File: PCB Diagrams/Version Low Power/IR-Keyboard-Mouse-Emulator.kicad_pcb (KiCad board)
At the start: 2 copper layers, 61 x 38.1 mm, 17 parts, among them J1 USB_A, J2 01x02, Q1 2N7000, Q2 BC547, U1 Arduino_Pro_Micro, U2 VS1838B

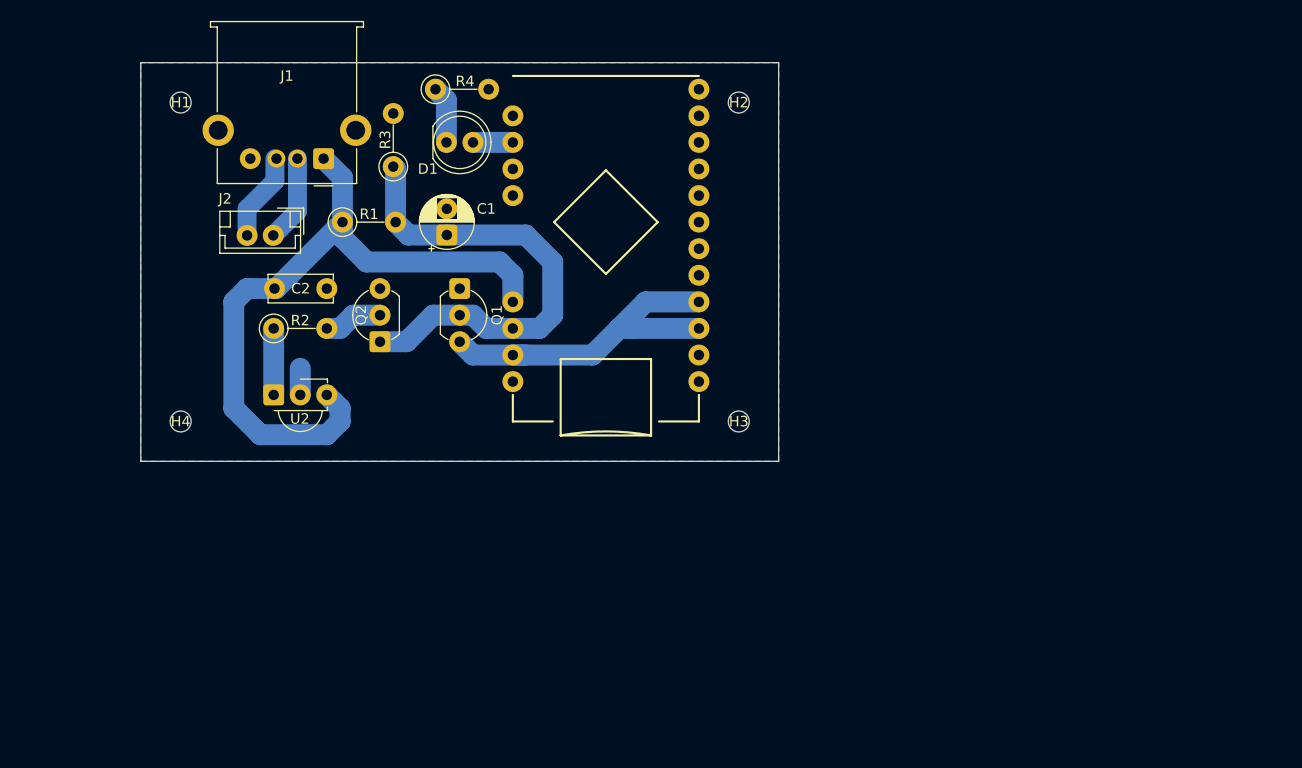
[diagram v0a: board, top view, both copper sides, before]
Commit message: Adding low-power firmware
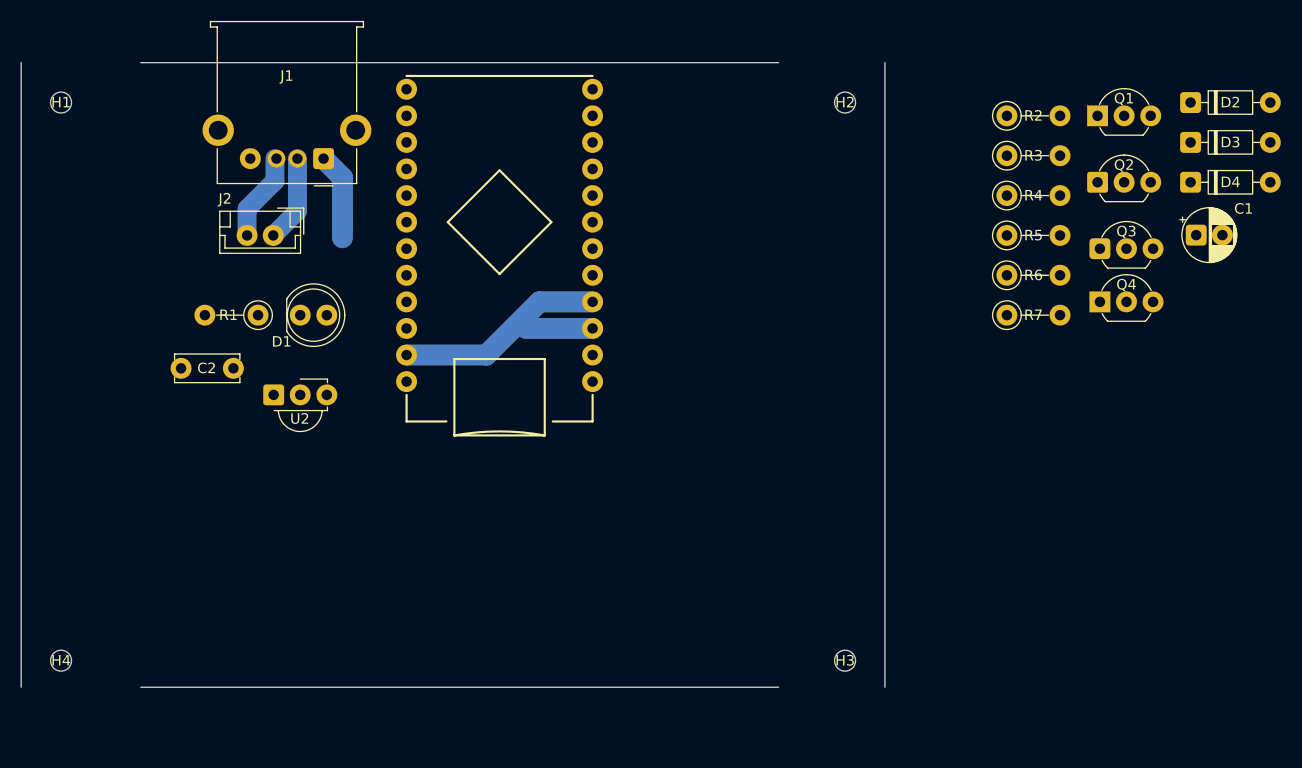
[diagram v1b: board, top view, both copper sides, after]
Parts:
- removed the R1 at (122.1, 64.8)
- added D2: 1N5817, Diode_THT:D_DO-35_SOD27_P7.62mm_Horizontal, F.Cu at (203.2, 53.3)
- added D3: 1N5817, Diode_THT:D_DO-35_SOD27_P7.62mm_Horizontal, F.Cu at (203.2, 57.1)
- added D4: 1N5817, Diode_THT:D_DO-35_SOD27_P7.62mm_Horizontal, F.Cu at (203.2, 61.0)
- added Q3: BC557, Package_TO_SOT_THT:TO-92_Inline_Wide, F.Cu at (194.5, 67.3)
- added Q4: BC547, Package_TO_SOT_THT:TO-92_Inline_Wide, F.Cu at (194.5, 72.4)
- added R4: 100K, Resistor_THT:R_Axial_DIN0207_L6.3mm_D2.5mm_P5.08mm_Vertical, F.Cu at (185.6, 62.2)
- added R5: 10K, Resistor_THT:R_Axial_DIN0207_L6.3mm_D2.5mm_P5.08mm_Vertical, F.Cu at (185.6, 66.0)
- added R6: 4.7K, Resistor_THT:R_Axial_DIN0207_L6.3mm_D2.5mm_P5.08mm_Vertical, F.Cu at (185.6, 69.8)
- added R7: 4.7K, Resistor_THT:R_Axial_DIN0207_L6.3mm_D2.5mm_P5.08mm_Vertical, F.Cu at (185.6, 73.7)
- C1: value 22uF -> 10uF
- Q1: value 2N7000 -> BC557
- R2: value 10K -> 47K
- R3: value 1M -> 10K
- moved R2 73.0 mm to (185.6, 54.6)
- moved C1 71.6 mm to (203.7, 66.0), turned to 0 degrees
- moved Q2 70.3 mm to (194.3, 61.0), turned to 0 degrees
- moved Q1 63.2 mm to (194.3, 54.6), turned to 0 degrees
- moved R3 58.7 mm to (185.6, 58.4), turned to 0 degrees
- moved R1 27.5 mm to (114.1, 73.7), turned to 180 degrees
- moved H4 25.6 mm to (95.2, 106.7)
- moved H3 25.0 mm to (170.2, 106.7)
- moved D1 21.6 mm to (118.1, 73.7)
- moved C2 15.9 mm to (106.7, 78.7), turned to 0 degrees
- moved H1 11.4 mm to (95.2, 53.3)
- moved H2 10.2 mm to (170.2, 53.3)
- moved U1 10.2 mm to (137.2, 67.3)
- renumbered R4 to R1
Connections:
- C1 pad 1: Net-(Q1-G) -> Net-(D4-A)
- Q1 pad 1: GND -> Net-(D4-A)
- Q1 pad 2: Net-(Q1-G) -> Net-(Q1-B)
- Q1 pad 3: GND_U1 -> +5V
- Q2 pad 1: Net-(Q1-G) -> Net-(Q2-C)
- Q2 pad 2: Net-(Q2-B) -> Net-(D2-K)
- R2 pad 2: Net-(Q2-B) -> Net-(Q1-B)
- R3 pad 1: Net-(Q1-G) -> Net-(D2-A)
- R3 pad 2: GND -> Net-(D4-A)
- U1 pad 21: +5V -> VCC
- U1 pad 23: GND_U1 -> GND
- U1 pad 3: GND_U1 -> GND
- U1 pad 4: GND_U1 -> GND
- U1 pad 7: unconnected-(U1-D4/A6-Pad7) -> DISCH
- U1 pad 8: unconnected-(U1-D5-Pad8) -> ON_OFF
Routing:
- net +5V: track 67.1 -> 8.31 mm
- net Net-(Q1-G): track 45.7 -> 0.00 mm
- net GND_U1: track 34.4 -> 0.00 mm
- net GND: track 2.54 -> 26.2 mm
- net IR_OUT: track 6.35 -> 0.00 mm
- net Net-(Q2-B): track 5.61 -> 0.00 mm
- net Net-(D1-K): track 5.51 -> 0.00 mm
- net Net-(D1-A): track 3.81 -> 0.00 mm
- removed copper zone on B.Cu, net GND
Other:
- board size 61 x 38.1 mm -> 82.6 x 59.7 mm

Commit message: Adding low-power version PCB
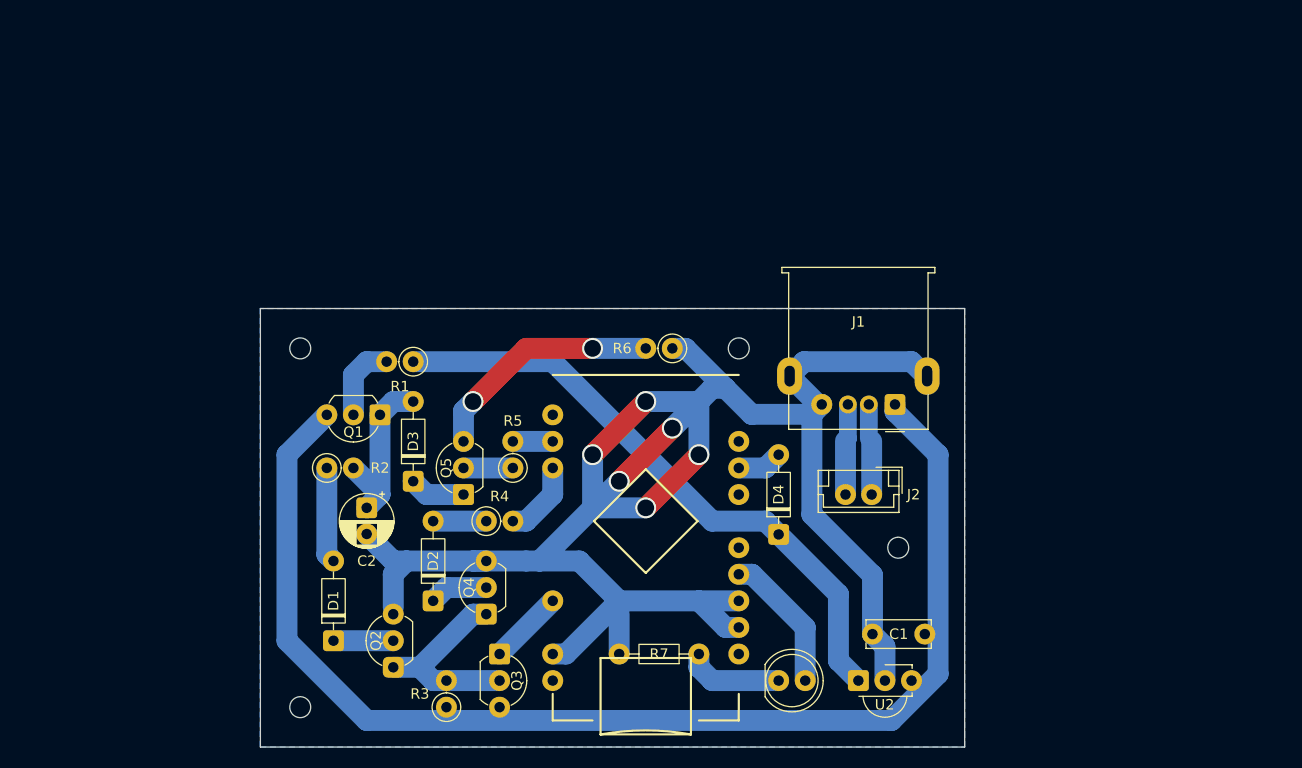
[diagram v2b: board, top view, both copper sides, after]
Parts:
- removed the R1 at (114.1, 73.7)
- added D5: LED, LED_THT:LED_D5.0mm, F.Cu at (163.8, 108.6)
- added Q5: BC547, Package_TO_SOT_THT:TO-92_Inline_Wide, F.Cu at (133.7, 90.8)
- added R2: 10K, Resistor_THT:R_Axial_DIN0207_L6.3mm_D2.5mm_P2.54mm_Vertical, F.Cu at (120.7, 88.3)
- C1: value 10uF -> 100nF; footprint Capacitor_THT:CP_Radial_D5.0mm_P2.50mm -> Capacitor_THT:C_Disc_D6.0mm_W2.5mm_P5.00mm
- C2: value 100nF -> 10uF; footprint Capacitor_THT:C_Disc_D6.0mm_W2.5mm_P5.00mm -> Capacitor_THT:CP_Radial_D5.0mm_P2.50mm
- D1: value LED -> 1N4148; footprint LED_THT:LED_D5.0mm -> Diode_THT:D_DO-35_SOD27_P7.62mm_Horizontal
- D2, D3, D4: value 1N5817 -> 1N4148
- R1: renamed from R2; footprint Resistor_THT:R_Axial_DIN0207_L6.3mm_D2.5mm_P5.08mm_Vertical -> Resistor_THT:R_Axial_DIN0207_L6.3mm_D2.5mm_P2.54mm_Vertical
- R3: value 10K -> 100K; footprint Resistor_THT:R_Axial_DIN0207_L6.3mm_D2.5mm_P5.08mm_Vertical -> Resistor_THT:R_Axial_DIN0207_L6.3mm_D2.5mm_P2.54mm_Vertical
- R4: value 100K -> 10K; footprint Resistor_THT:R_Axial_DIN0207_L6.3mm_D2.5mm_P5.08mm_Vertical -> Resistor_THT:R_Axial_DIN0207_L6.3mm_D2.5mm_P2.54mm_Vertical
- R5: value 10K -> 4.7K; footprint Resistor_THT:R_Axial_DIN0207_L6.3mm_D2.5mm_P5.08mm_Vertical -> Resistor_THT:R_Axial_DIN0207_L6.3mm_D2.5mm_P2.54mm_Vertical
- R6: footprint Resistor_THT:R_Axial_DIN0207_L6.3mm_D2.5mm_P5.08mm_Vertical -> Resistor_THT:R_Axial_DIN0207_L6.3mm_D2.5mm_P2.54mm_Vertical
- R7: value 4.7K -> 1K; footprint Resistor_THT:R_Axial_DIN0207_L6.3mm_D2.5mm_P5.08mm_Vertical -> Resistor_THT:R_Axial_DIN0204_L3.6mm_D1.6mm_P7.62mm_Horizontal
- moved D2 86.7 mm to (130.8, 101.0), turned to 90 degrees
- moved Q2 81.7 mm to (127.0, 107.3), turned to 90 degrees
- moved D3 81.0 mm to (128.9, 89.5), turned to 90 degrees
- moved R3 75.1 mm to (132.1, 111.1), turned to 90 degrees
- moved Q1 74.3 mm to (125.7, 83.2), turned to 180 degrees
- moved Q3 69.2 mm to (137.2, 106.0), turned to -90 degrees
- moved Q4 65.8 mm to (135.9, 102.2), turned to 90 degrees
- moved J2 62.3 mm to (172.7, 90.8)
- moved U2 62.2 mm to (171.4, 108.6)
- moved R1 61.4 mm to (128.9, 78.1), turned to 180 degrees
- moved J1 59.4 mm to (174.9, 82.2)
- moved R4 58.7 mm to (135.9, 93.3)
- moved R5 52.2 mm to (138.4, 88.3), turned to 90 degrees
- moved D4 51.8 mm to (163.8, 94.6), turned to 90 degrees
- moved C1 49.1 mm to (172.8, 104.1)
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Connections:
- C1 pad 1: Net-(D4-A) -> GND
- C1 pad 2: GND -> +5V
- C2 pad 1: GND -> Net-(D3-A)
- C2 pad 2: +5V -> GND
- D3 pad 1: Net-(D2-K) -> Net-(D3-K)
- D4 pad 1: Net-(D4-K) -> IR_OUT
- Q1 pad 1: Net-(D4-A) -> Net-(D3-A)
- Q2 pad 2: Net-(D2-K) -> Net-(D1-K)
- Q4 pad 1: Net-(D4-K) -> Net-(Q2-C)
- Q4 pad 2: Net-(Q4-B) -> Net-(D2-K)
- Q4 pad 3: Net-(Q4-E) -> GND
- R3 pad 1: Net-(D2-A) -> +5V
- R3 pad 2: Net-(D4-A) -> Net-(Q2-C)
- R4 pad 1: +5V -> Net-(D2-A)
- R4 pad 2: Net-(Q2-C) -> ON_OFF
- R5 pad 1: Net-(D3-A) -> Net-(Q5-B)
- R5 pad 2: ON_OFF -> DISCH
- R6 pad 1: DISCH -> GND
- R6 pad 2: Net-(Q4-B) -> Net-(Q5-E)
- R7 pad 1: GND -> Net-(D5-K)
- R7 pad 2: Net-(Q4-E) -> GND
- U1 pad 15: Net-(D1-A) -> DISCH
- U1 pad 16: unconnected-(U1-D15-Pad16) -> ON_OFF
- U1 pad 2: unconnected-(U1-RX-Pad2) -> (no net)
- U1 pad 5: unconnected-(U1-D2-Pad5) -> LED
- U1 pad 8: ON_OFF -> unconnected-(U1-D5-Pad8)
- U1 pad 9: unconnected-(U1-D6/A7-Pad9) -> Net-(D4-A)
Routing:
- net GND: track 26.2 -> 185.0 mm, vias 0 -> 6
- net +5V: track 8.31 -> 117.9 mm
- net IR_OUT: track 0.00 -> 58.9 mm
- net Net-(Q5-E): track 0.00 -> 22.8 mm, vias 0 -> 2
- net Net-(Q2-C): track 0.00 -> 19.1 mm
- net Net-(D3-A): track 0.00 -> 16.7 mm
- net LED: track 0.00 -> 13.5 mm
- net Net-(D5-K): track 0.00 -> 9.42 mm
- net Net-(D1-A): track 0.00 -> 9.15 mm
- net Net-(Q1-B): track 0.00 -> 7.51 mm
- net VCC: track 0.00 -> 7.18 mm
- net ON_OFF: track 0.00 -> 7.18 mm
- net Net-(D2-K): track 0.00 -> 5.61 mm
- net Net-(D3-K): track 0.00 -> 5.33 mm
- net Net-(D1-K): track 0.00 -> 5.08 mm
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- added copper zone on B.Cu, net GND
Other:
- board size 82.6 x 59.7 mm -> 67.3 x 41.9 mm
